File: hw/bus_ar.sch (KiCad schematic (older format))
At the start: 5 parts, among them U901 74HC541, U902 74HC541, U903 74HC245, U904 74HC574, U905 74HC574

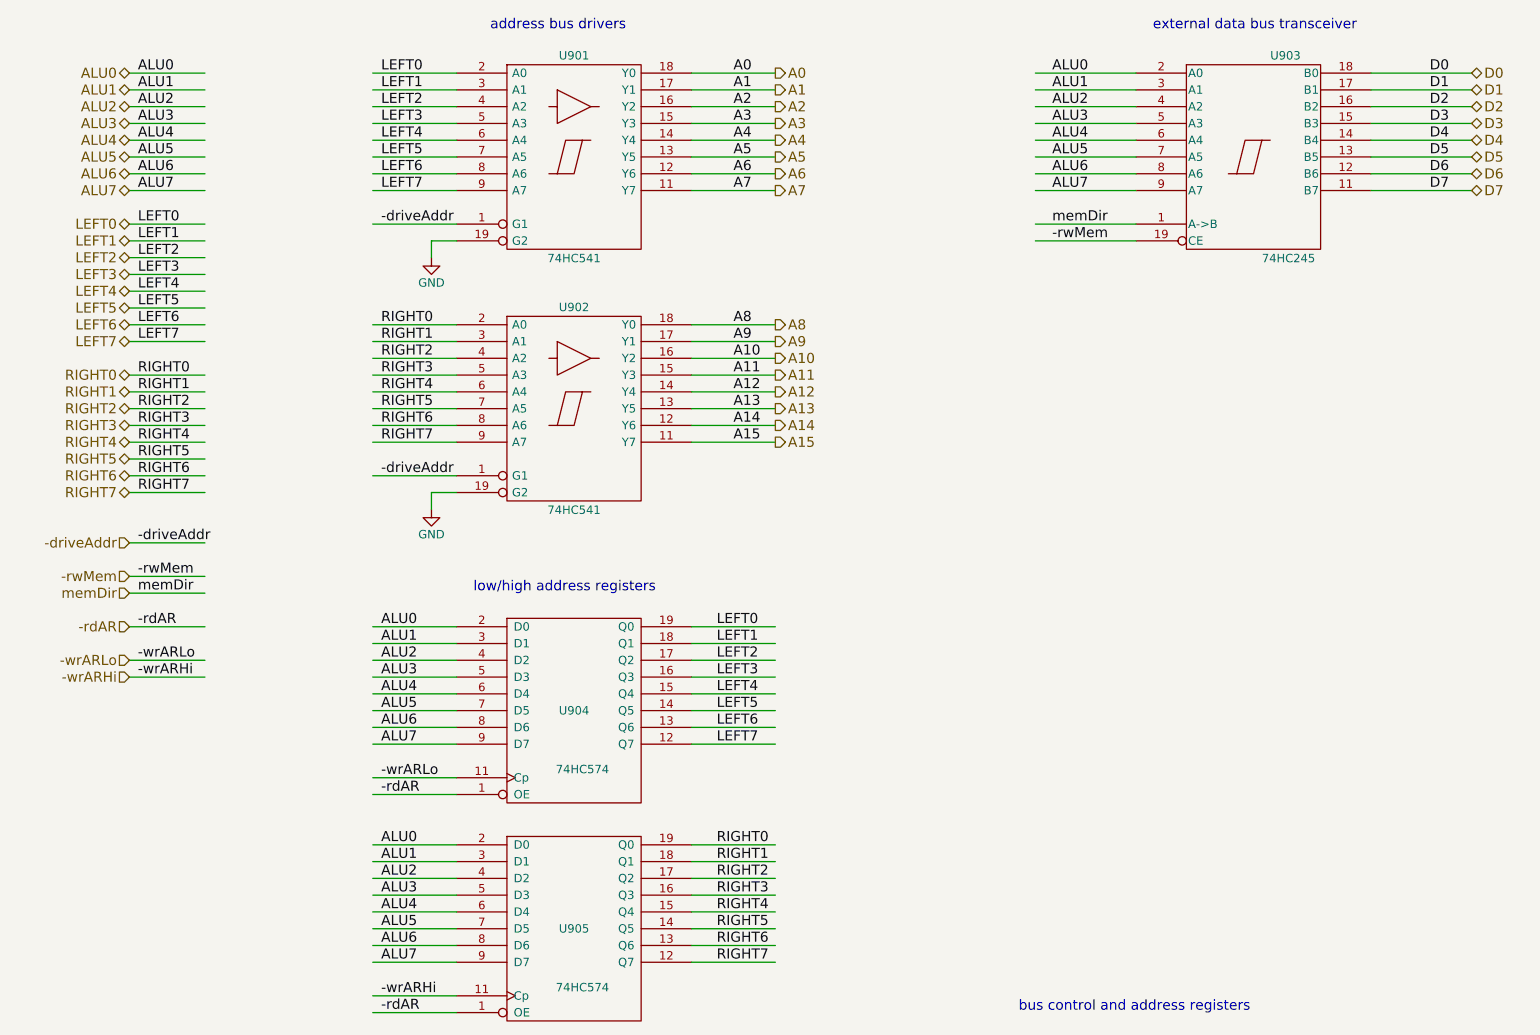
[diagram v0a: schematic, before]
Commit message: have AR regs output to the low/high addr busses
For store instructions, a GP register pair is used
to specify the address, AND a GP register specifies
the data.  This means we can't drive the address
bus directly from a GP register pair, since that
wouldn't allow us to output the correct data.  So,
the contents of the GP register pair specifying the
address must be transferred into the AR registers,
which can then drive the address, allowing the
correct GP register data to be output via the ALU.

Will need to add a microcode signal for driving the
address bus from the AR registers.
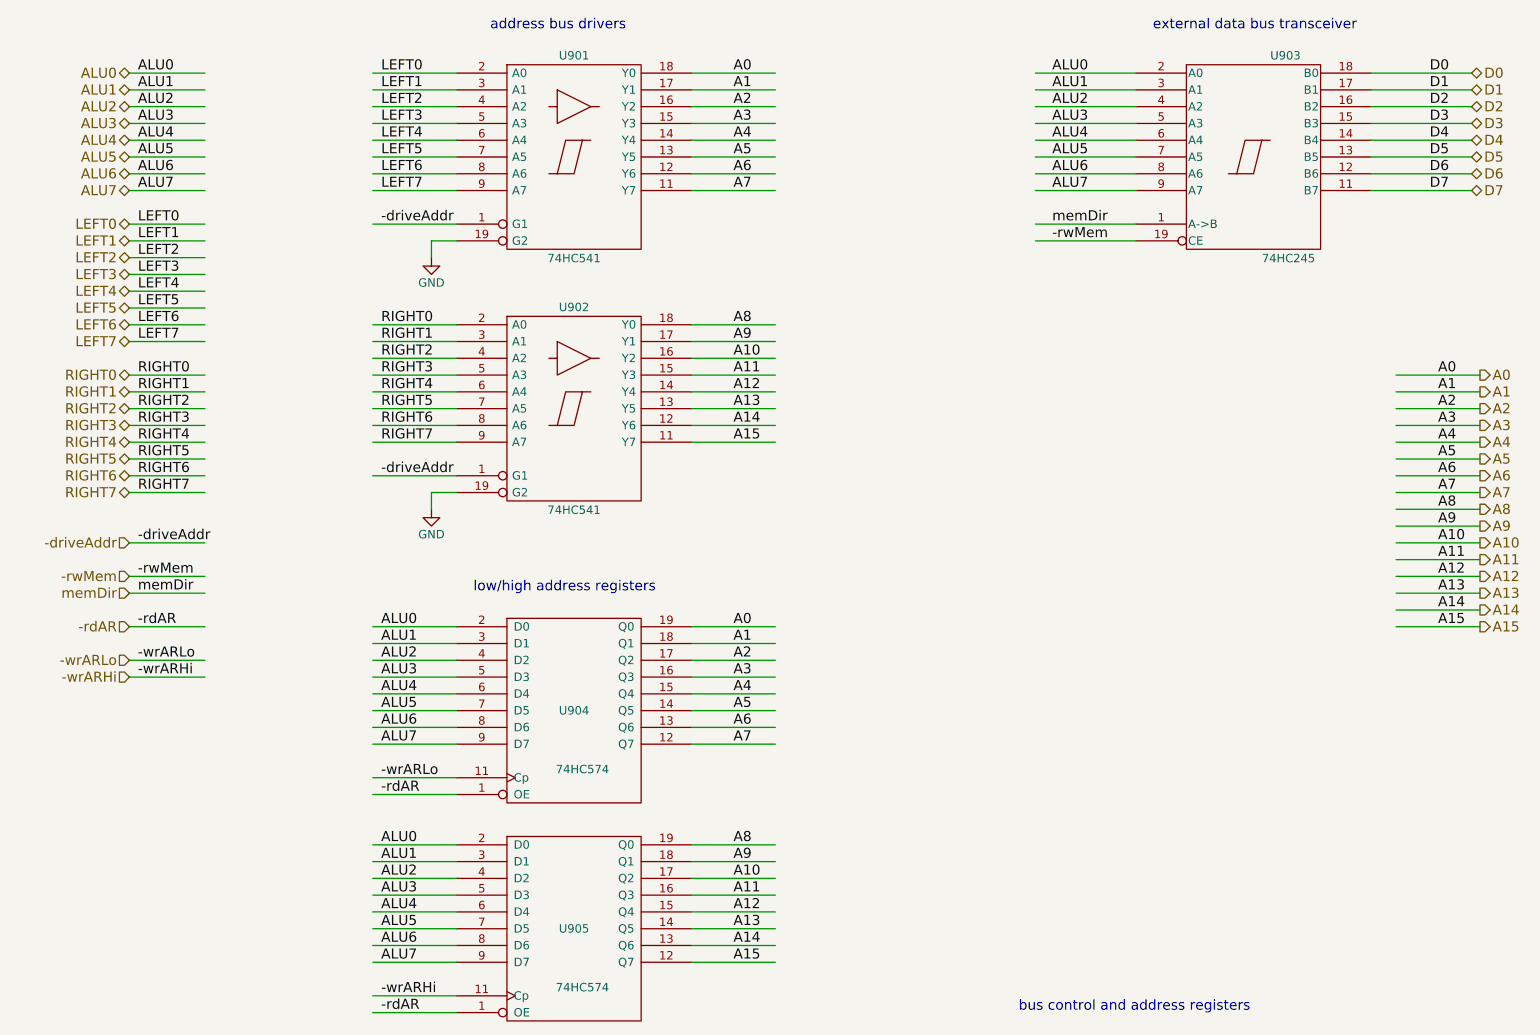
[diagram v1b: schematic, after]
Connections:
- wire segments 122 -> 138
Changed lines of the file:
@@
 Wire Wire Line
 	3800 6500 3300 6500
-Wire Wire Line
-	5700 4500 5200 4500
-Wire Wire Line
-	5700 4600 5200 4600
-Wire Wire Line
-	5700 4700 5200 4700
-Wire Wire Line
-	5700 4800 5200 4800
-Wire Wire Line
-	5700 4900 5200 4900
-Wire Wire Line
-	5700 5000 5200 5000
-Wire Wire Line
-	5700 5100 5200 5100
-Wire Wire Line
-	5700 5200 5200 5200
-Wire Wire Line
-	5700 5800 5200 5800
-Wire Wire Line
-	5700 5900 5200 5900
-Wire Wire Line
-	5700 6000 5200 6000
-Wire Wire Line
-	5700 6100 5200 6100
-Wire Wire Line
-	5700 6200 5200 6200
-Wire Wire Line
-	5700 6300 5200 6300
-Wire Wire Line
-	5700 6400 5200 6400
-Wire Wire Line
-	5700 6500 5200 6500
 Text Label 3350 4500 0    60   ~ 0
 ALU0
@@
 Text Label 3350 6500 0    60   ~ 0
 ALU7
-Text Label 5350 4500 0    60   ~ 0
-LEFT0
-Text Label 5350 4600 0    60   ~ 0
-LEFT1
-Text Label 5350 4700 0    60   ~ 0
-LEFT2
-Text Label 5350 4800 0    60   ~ 0
-LEFT3
-Text Label 5350 4900 0    60   ~ 0
-LEFT4
-Text Label 5350 5000 0    60   ~ 0
-LEFT5
-Text Label 5350 5100 0    60   ~ 0
-LEFT6
-Text Label 5350 5200 0    60   ~ 0
-LEFT7
-Text Label 5350 5800 0    60   ~ 0
-RIGHT0
-Text Label 5350 5900 0    60   ~ 0
-RIGHT1
-Text Label 5350 6000 0    60   ~ 0
-RIGHT2
-Text Label 5350 6100 0    60   ~ 0
-RIGHT3
-Text Label 5350 6200 0    60   ~ 0
-RIGHT4
-Text Label 5350 6300 0    60   ~ 0
-RIGHT5
-Text Label 5350 6400 0    60   ~ 0
-RIGHT6
-Text Label 5350 6500 0    60   ~ 0
-RIGHT7
 Wire Wire Line
 	1850 1200 2300 1200
@@
 Text HLabel 1850 4800 0    60   Input ~ 0
 -wrARHi
-Text HLabel 5700 1200 2    60   Output ~ 0
+Text HLabel 9900 3000 2    60   Output ~ 0
 A0
-Text HLabel 5700 1300 2    60   Output ~ 0
+Text HLabel 9900 3100 2    60   Output ~ 0
 A1
-Text HLabel 5700 1400 2    60   Output ~ 0
+Text HLabel 9900 3200 2    60   Output ~ 0
 A2
-Text HLabel 5700 1500 2    60   Output ~ 0
+Text HLabel 9900 3300 2    60   Output ~ 0
 A3
-Text HLabel 5700 1600 2    60   Output ~ 0
+Text HLabel 9900 3400 2    60   Output ~ 0
 A4
-Text HLabel 5700 1700 2    60   Output ~ 0
+Text HLabel 9900 3500 2    60   Output ~ 0
 A5
-Text HLabel 5700 1800 2    60   Output ~ 0
+Text HLabel 9900 3600 2    60   Output ~ 0
 A6
-Text HLabel 5700 1900 2    60   Output ~ 0
+Text HLabel 9900 3700 2    60   Output ~ 0
 A7
-Text HLabel 5700 2700 2    60   Output ~ 0
+Text HLabel 9900 3800 2    60   Output ~ 0
 A8
-Text HLabel 5700 2800 2    60   Output ~ 0
+Text HLabel 9900 3900 2    60   Output ~ 0
 A9
-Text HLabel 5700 2900 2    60   Output ~ 0
+Text HLabel 9900 4000 2    60   Output ~ 0
 A10
-Text HLabel 5700 3000 2    60   Output ~ 0
+Text HLabel 9900 4100 2    60   Output ~ 0
 A11
-Text HLabel 5700 3100 2    60   Output ~ 0
+Text HLabel 9900 4200 2    60   Output ~ 0
 A12
-Text HLabel 5700 3200 2    60   Output ~ 0
+Text HLabel 9900 4300 2    60   Output ~ 0
 A13
-Text HLabel 5700 3300 2    60   Output ~ 0
+Text HLabel 9900 4400 2    60   Output ~ 0
 A14
-Text HLabel 5700 3400 2    60   Output ~ 0
+Text HLabel 9900 4500 2    60   Output ~ 0
 A15
 Text HLabel 9850 1200 2    60   BiDi ~ 0
@@
 Text Notes 3900 4300 0    60   ~ 0
 low/high address registers
+Wire Wire Line
+	5200 4500 5700 4500
+Wire Wire Line
+	5200 4600 5700 4600
+Wire Wire Line
+	5200 4700 5700 4700
+Wire Wire Line
+	5200 4800 5700 4800
+Wire Wire Line
+	5200 4900 5700 4900
+Wire Wire Line
+	5200 5000 5700 5000
+Wire Wire Line
+	5200 5100 5700 5100
+Wire Wire Line
+	5200 5200 5700 5200
+Wire Wire Line
+	5200 5800 5700 5800
+Wire Wire Line
+	5200 5900 5700 5900
+Wire Wire Line
+	5200 6000 5700 6000
+Wire Wire Line
+	5200 6100 5700 6100
+Wire Wire Line
+	5200 6200 5700 6200
+Wire Wire Line
+	5200 6300 5700 6300
+Wire Wire Line
+	5200 6400 5700 6400
+Wire Wire Line
+	5200 6500 5700 6500
+Text Label 5450 4500 0    60   ~ 0
+A0
+Text Label 5450 4600 0    60   ~ 0
+A1
+Text Label 5450 4700 0    60   ~ 0
+A2
+Text Label 5450 4800 0    60   ~ 0
+A3
+Text Label 5450 4900 0    60   ~ 0
+A4
+Text Label 5450 5000 0    60   ~ 0
+A5
+Text Label 5450 5100 0    60   ~ 0
+A6
+Text Label 5450 5200 0    60   ~ 0
+A7
+Text Label 5450 5800 0    60   ~ 0
+A8
+Text Label 5450 5900 0    60   ~ 0
+A9
+Text Label 5450 6000 0    60   ~ 0
+A10
+Text Label 5450 6100 0    60   ~ 0
+A11
+Text Label 5450 6200 0    60   ~ 0
+A12
+Text Label 5450 6300 0    60   ~ 0
+A13
+Text Label 5450 6400 0    60   ~ 0
+A14
+Text Label 5450 6500 0    60   ~ 0
+A15
+Wire Wire Line
+	9400 3000 9900 3000
+Wire Wire Line
+	9400 3100 9900 3100
+Wire Wire Line
+	9400 3200 9900 3200
+Wire Wire Line
+	9400 3300 9900 3300
+Wire Wire Line
+	9400 3400 9900 3400
+Wire Wire Line
+	9400 3500 9900 3500
+Wire Wire Line
+	9400 3600 9900 3600
+Wire Wire Line
+	9400 3700 9900 3700
+Wire Wire Line
+	9400 3800 9900 3800
+Wire Wire Line
+	9400 3900 9900 3900
+Wire Wire Line
+	9400 4000 9900 4000
+Wire Wire Line
+	9400 4100 9900 4100
+Wire Wire Line
+	9400 4200 9900 4200
+Wire Wire Line
+	9400 4300 9900 4300
+Wire Wire Line
+	9400 4400 9900 4400
+Wire Wire Line
+	9400 4500 9900 4500
+Text Label 9650 3000 0    60   ~ 0
+A0
+Text Label 9650 3100 0    60   ~ 0
+A1
+Text Label 9650 3200 0    60   ~ 0
+A2
+Text Label 9650 3300 0    60   ~ 0
+A3
+Text Label 9650 3400 0    60   ~ 0
+A4
+Text Label 9650 3500 0    60   ~ 0
+A5
+Text Label 9650 3600 0    60   ~ 0
+A6
+Text Label 9650 3700 0    60   ~ 0
+A7
+Text Label 9650 3800 0    60   ~ 0
+A8
+Text Label 9650 3900 0    60   ~ 0
+A9
+Text Label 9650 4000 0    60   ~ 0
+A10
+Text Label 9650 4100 0    60   ~ 0
+A11
+Text Label 9650 4200 0    60   ~ 0
+A12
+Text Label 9650 4300 0    60   ~ 0
+A13
+Text Label 9650 4400 0    60   ~ 0
+A14
+Text Label 9650 4500 0    60   ~ 0
+A15
 $EndSCHEMATC

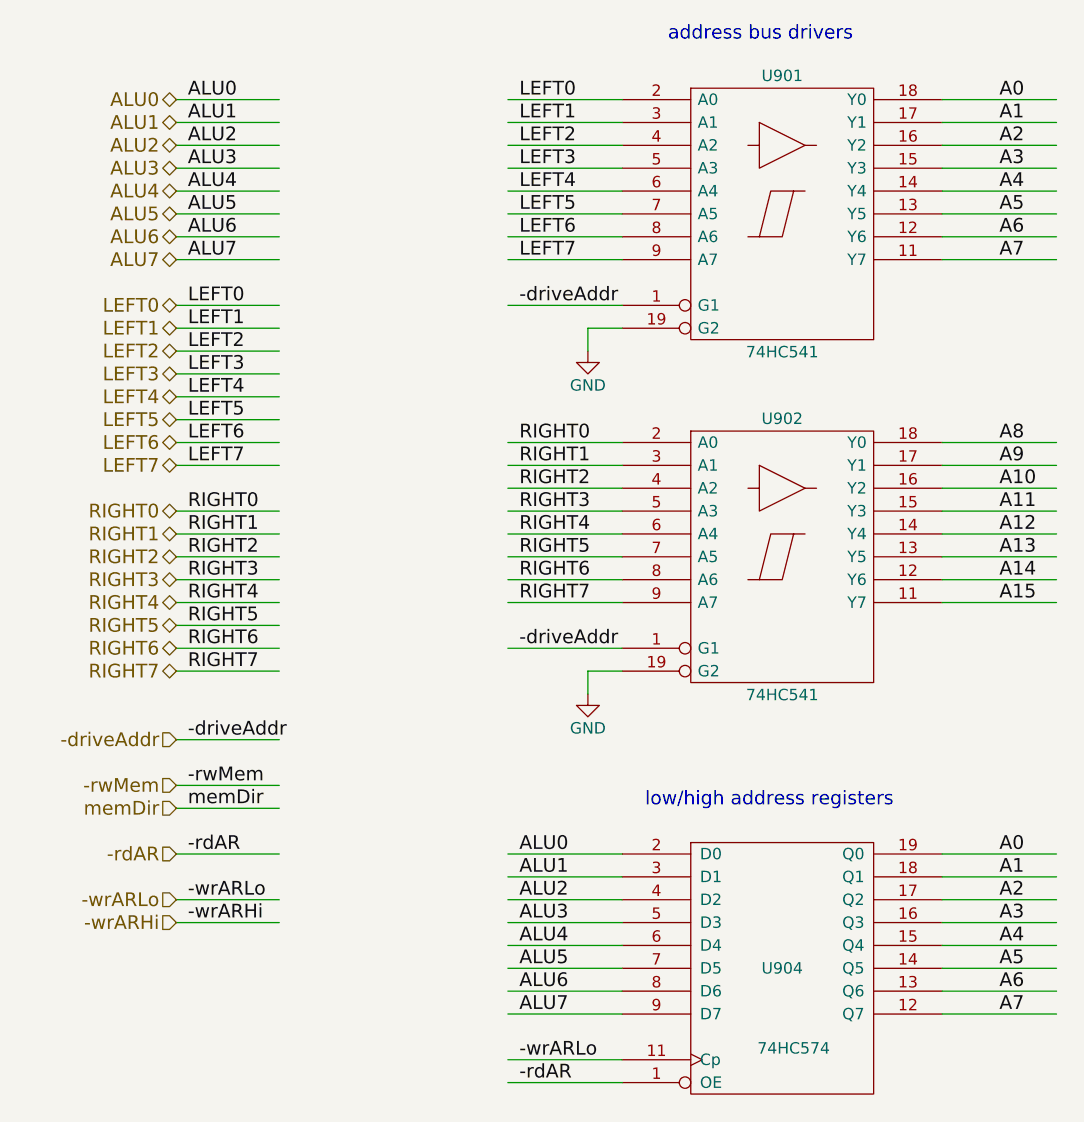
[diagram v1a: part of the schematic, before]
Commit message: use '573 latches as address bus drivers
This let's us latch the address being asserted onto
the left/right ALU inputs busses in case it is going
to change during the execution of the instruction.
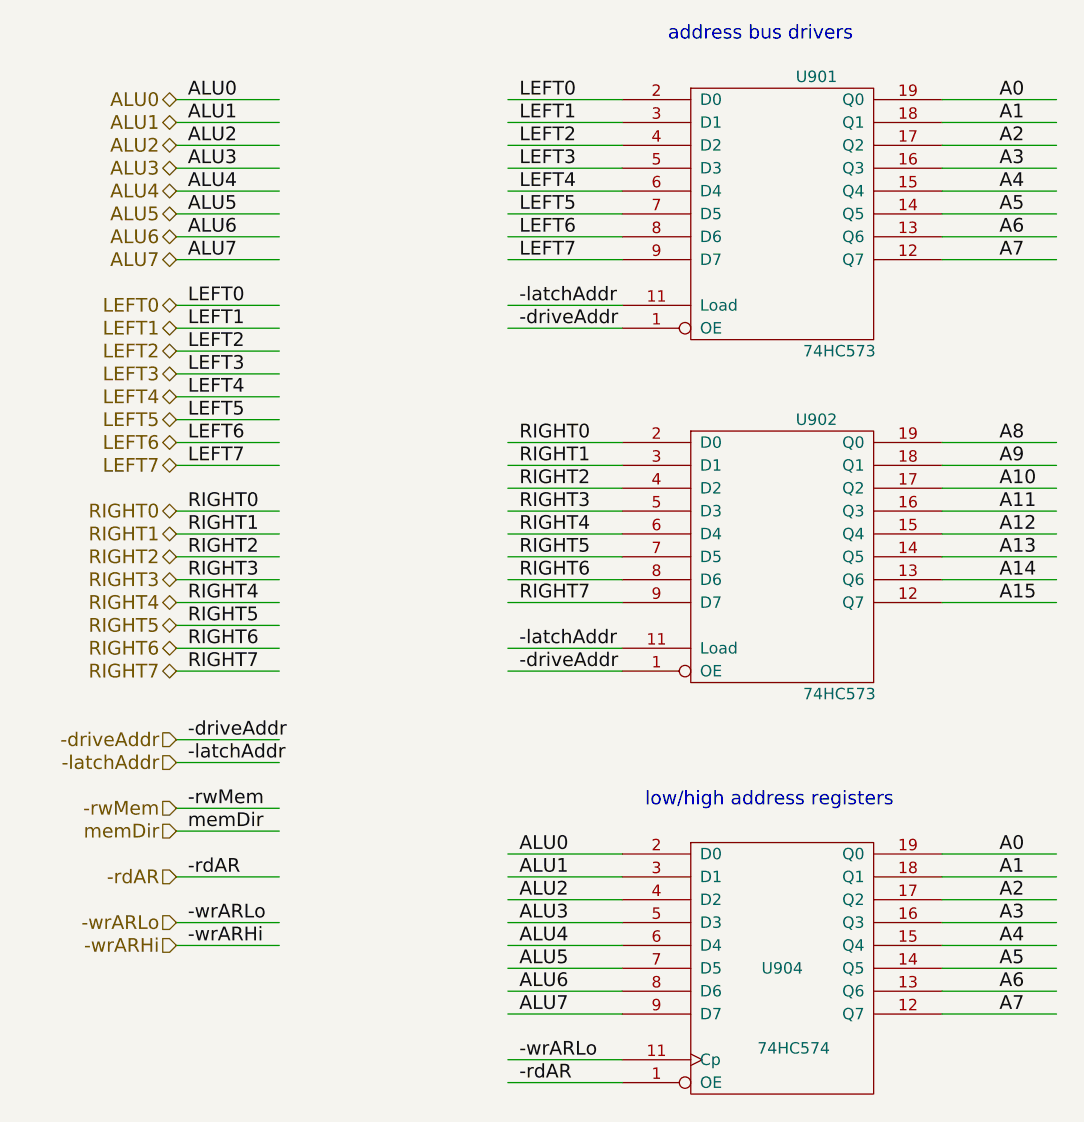
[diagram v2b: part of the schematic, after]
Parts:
- removed U901, U902: 74HC541, symbol 74LS541
- added U901, U902: 74HC573, symbol 74LS573
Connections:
- net labels added: -latchAddr
- net labels removed: GND
- wire segments 138 -> 137
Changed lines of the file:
@@
 Text Notes 7150 6800 0    60   ~ 0
 bus control and address registers
-$Comp
-L 74LS541 U901
-U 1 1 595E91CD
-P 4500 1700
-F 0 "U901" H 4500 2275 50  0000 C BNN
-F 1 "74HC541" H 4500 1125 50  0000 C TNN
-F 2 "" H 4500 1700 50  0001 C CNN
-F 3 "" H 4500 1700 50  0001 C CNN
-	1    4500 1700
-	1    0    0    -1
-$EndComp
-$Comp
-L 74LS541 U902
-U 1 1 595E9238
-P 4500 3200
-F 0 "U902" H 4500 3775 50  0000 C BNN
-F 1 "74HC541" H 4500 2625 50  0000 C TNN
-F 2 "" H 4500 3200 50  0001 C CNN
-F 3 "" H 4500 3200 50  0001 C CNN
-	1    4500 3200
-	1    0    0    -1
-$EndComp
 Wire Wire Line
 	3800 1200 3300 1200
@@
 	3800 1900 3300 1900
 Wire Wire Line
-	3800 2200 3650 2200
-Wire Wire Line
-	3650 2200 3650 2300
-Wire Wire Line
-	3800 2100 3300 2100
-$Comp
-L GND #PWR?
-U 1 1 595E928D
-P 3650 2300
-F 0 "#PWR?" H 3650 2050 50  0001 C CNN
-F 1 "GND" H 3650 2150 50  0000 C CNN
-F 2 "" H 3650 2300 50  0001 C CNN
-F 3 "" H 3650 2300 50  0001 C CNN
-	1    3650 2300
-	1    0    0    -1
-$EndComp
+	3800 2200 3300 2200
 Wire Wire Line
 	3800 2700 3300 2700
@@
 	3800 3400 3300 3400
 Wire Wire Line
-	3800 3700 3650 3700
-Wire Wire Line
-	3650 3700 3650 3800
-Wire Wire Line
-	3800 3600 3300 3600
-$Comp
-L GND #PWR?
-U 1 1 595E92CA
-P 3650 3800
-F 0 "#PWR?" H 3650 3550 50  0001 C CNN
-F 1 "GND" H 3650 3650 50  0000 C CNN
-F 2 "" H 3650 3800 50  0001 C CNN
-F 3 "" H 3650 3800 50  0001 C CNN
-	1    3650 3800
-	1    0    0    -1
-$EndComp
+	3800 3700 3300 3700
 Text Label 3350 1200 0    60   ~ 0
 LEFT0
@@
 Text Label 3350 3400 0    60   ~ 0
 RIGHT7
-Text Label 3350 2100 0    60   ~ 0
+Text Label 3350 2200 0    60   ~ 0
 -driveAddr
-Text Label 3350 3600 0    60   ~ 0
+Text Label 3350 3700 0    60   ~ 0
 -driveAddr
 Wire Wire Line
@@
 	1850 4000 2300 4000
 Wire Wire Line
-	1850 4200 2300 4200
-Wire Wire Line
 	1850 4300 2300 4300
 Wire Wire Line
-	1850 4500 2300 4500
-Wire Wire Line
-	1850 4700 2300 4700
+	1850 4400 2300 4400
+Wire Wire Line
+	1850 4600 2300 4600
 Wire Wire Line
 	1850 4800 2300 4800
+Wire Wire Line
+	1850 4900 2300 4900
 Text Label 1900 4000 0    60   ~ 0
 -driveAddr
-Text Label 1900 4200 0    60   ~ 0
+Text Label 1900 4300 0    60   ~ 0
 -rwMem
 Wire Wire Line
@@
 Text Label 7350 2100 0    60   ~ 0
 memDir
-Text Label 1900 4300 0    60   ~ 0
+Text Label 1900 4400 0    60   ~ 0
 memDir
 Wire Wire Line
@@
 Text Label 3350 6800 0    60   ~ 0
 -rdAR
-Text Label 1900 4500 0    60   ~ 0
+Text Label 1900 4600 0    60   ~ 0
 -rdAR
-Text Label 1900 4700 0    60   ~ 0
+Text Label 1900 4800 0    60   ~ 0
 -wrARLo
-Text Label 1900 4800 0    60   ~ 0
+Text Label 1900 4900 0    60   ~ 0
 -wrARHi
 Text HLabel 1850 1200 0    60   BiDi ~ 0
@@
 Text HLabel 1850 4000 0    60   Input ~ 0
 -driveAddr
-Text HLabel 1850 4200 0    60   Input ~ 0
+Text HLabel 1850 4300 0    60   Input ~ 0
 -rwMem
-Text HLabel 1850 4300 0    60   Input ~ 0
+Text HLabel 1850 4400 0    60   Input ~ 0
 memDir
-Text HLabel 1850 4500 0    60   Input ~ 0
+Text HLabel 1850 4600 0    60   Input ~ 0
 -rdAR
-Text HLabel 1850 4700 0    60   Input ~ 0
+Text HLabel 1850 4800 0    60   Input ~ 0
 -wrARLo
-Text HLabel 1850 4800 0    60   Input ~ 0
+Text HLabel 1850 4900 0    60   Input ~ 0
 -wrARHi
 Text HLabel 9900 3000 2    60   Output ~ 0
@@
 Text Label 9650 4500 0    60   ~ 0
 A15
+$Comp
+L 74LS573 U901
+U 1 1 59676DEE
+P 4500 1700
+F 0 "U901" H 4650 2300 50  0000 C CNN
+F 1 "74HC573" H 4750 1100 50  0000 C CNN
+F 2 "" H 4500 1700 50  0001 C CNN
+F 3 "" H 4500 1700 50  0001 C CNN
+	1    4500 1700
+	1    0    0    -1
+$EndComp
+$Comp
+L 74LS573 U902
+U 1 1 59676E71
+P 4500 3200
+F 0 "U902" H 4650 3800 50  0000 C CNN
+F 1 "74HC573" H 4750 2600 50  0000 C CNN
+F 2 "" H 4500 3200 50  0001 C CNN
+F 3 "" H 4500 3200 50  0001 C CNN
+	1    4500 3200
+	1    0    0    -1
+$EndComp
+Wire Wire Line
+	3800 2100 3300 2100
+Wire Wire Line
+	3800 3600 3300 3600
+Text Label 3350 2100 0    60   ~ 0
+-latchAddr
+Text Label 3350 3600 0    60   ~ 0
+-latchAddr
+Wire Wire Line
+	1850 4100 2300 4100
+Text Label 1900 4100 0    60   ~ 0
+-latchAddr
+Text HLabel 1850 4100 0    60   Input ~ 0
+-latchAddr
 $EndSCHEMATC
